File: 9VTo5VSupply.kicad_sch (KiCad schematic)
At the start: 13 parts, among them U3 MC33063AP

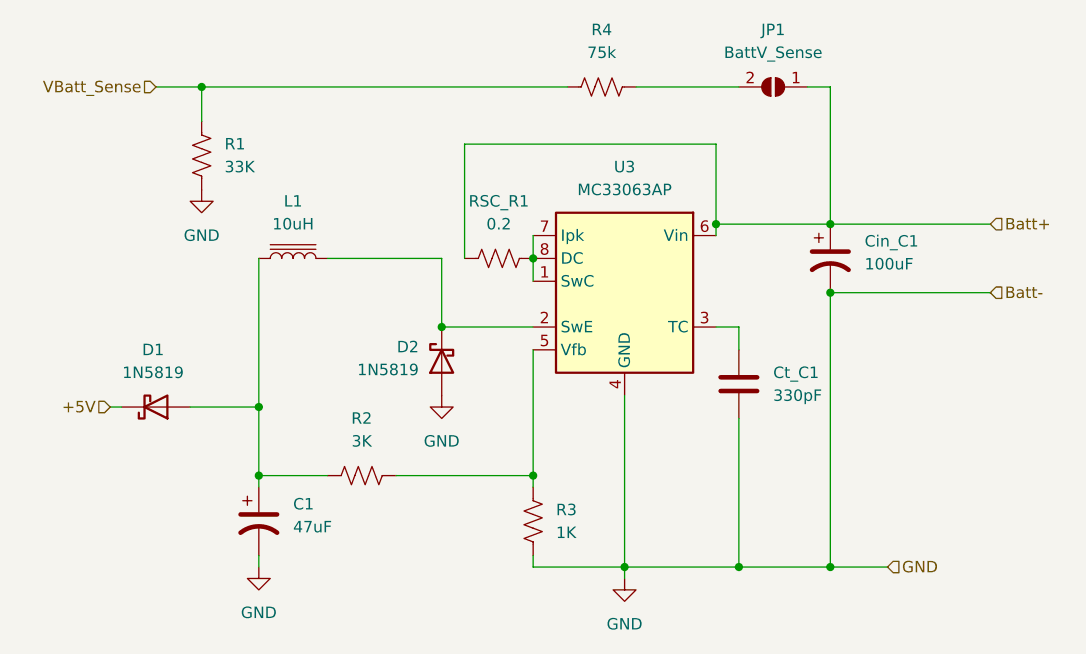
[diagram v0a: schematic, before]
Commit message: WIP: Updating board to use an RP2040 directly.
TODO: Need to update on-board LEDs to SK6812 Mini-E, fix VSYS/VBUS/+5V, and convert any footprints of interest to SMD
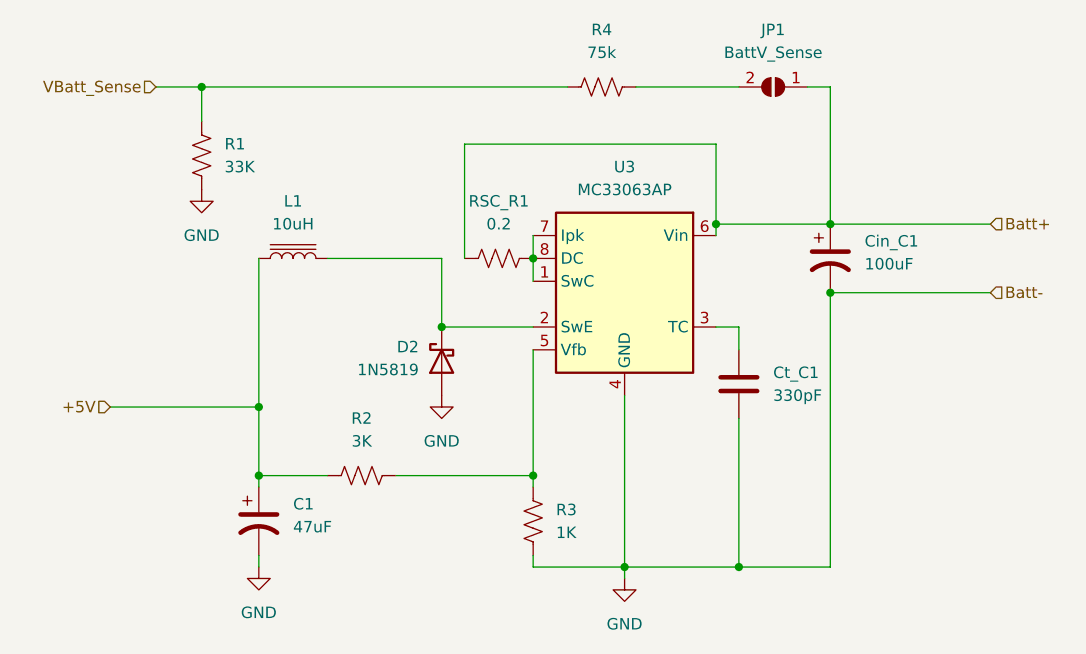
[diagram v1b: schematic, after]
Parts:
- removed D1: 1N5819, Diode_THT:D_DO-41_SOD81_P10.16mm_Horizontal, symbol Diode:1N5819
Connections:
- net +5V: now also C1.1, L1.2, R2.1
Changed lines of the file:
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@@
-	)
-	(junction
-		(at 180.34 111.76)
-		(diameter 0)
-		(color 0 0 0 0)
 	)
 	(junction
@@
 	(wire
 		(pts
-			(xy 180.34 111.76) (xy 186.69 111.76)
-		)
-		(stroke
-			(width 0)
-			(type default)
-		)
-	)
-	(wire
-		(pts
 			(xy 132.08 101.6) (xy 147.32 101.6)
 		)
@@
 	(wire
 		(pts
-			(xy 100.33 93.98) (xy 101.6 93.98)
+			(xy 100.33 93.98) (xy 116.84 93.98)
 		)
 		(stroke
@@
 		(pts
 			(xy 170.18 111.76) (xy 180.34 111.76)
-		)
-		(stroke
-			(width 0)
-			(type default)
-		)
-	)
-	(wire
-		(pts
-			(xy 109.22 93.98) (xy 116.84 93.98)
 		)
 		(stroke
@@
 		(shape input)
 		(at 198.12 73.66 0)
-		(fields_autoplaced yes)
-		(effects
-			(font
-				(size 1.27 1.27)
-			)
-			(justify left)
-		)
-	)
-	(hierarchical_label "GND"
-		(shape input)
-		(at 186.69 111.76 0)
 		(fields_autoplaced yes)
 		(effects
@@
 					(unit 1)
 				)
-			)
-		)
-	)
-	(symbol
-		(lib_id "Diode:1N5819")
-		(at 105.41 93.98 0)
-		(mirror x)
-		(unit 1)
-		(exclude_from_sim no)
-		(in_bom yes)
-		(on_board yes)
-		(dnp no)
-		(fields_autoplaced yes)
-		(property "Reference" "D1"
-			(at 105.0925 87.63 0)
-			(effects
-				(font
-					(size 1.27 1.27)
-				)
-			)
-		)
-		(property "Value" "1N5819"
-			(at 105.0925 90.17 0)
-			(effects
-				(font
-					(size 1.27 1.27)
-				)
-			)
-		)
-		(property "Footprint" "Diode_THT:D_DO-41_SOD81_P10.16mm_Horizontal"
-			(at 105.41 89.535 0)
-			(effects
-				(font
-					(size 1.27 1.27)
-				)
-				(hide yes)
-			)
-		)
-		(property "Datasheet" "http://www.vishay.com/docs/88525/1n5817.pdf"
-			(at 105.41 93.98 0)
-			(effects
-				(font
-					(size 1.27 1.27)
-				)
-				(hide yes)
-			)
-		)
-		(property "Description" ""
-			(at 105.41 93.98 0)
-			(effects
-				(font
-					(size 1.27 1.27)
-				)
-				(hide yes)
-			)
-		)
-		(pin "1"
-		)
-		(pin "2"
-		)
-		(instances
-			(project "WeddingCenterPieces"
-				(path "/4e0ee48d-0121-4621-a533-4795bdfb88f1/5e4c62e3-b615-407a-9cf1-a60a2c093e49"
-					(reference "D1")
-					(unit 1)
-				)
